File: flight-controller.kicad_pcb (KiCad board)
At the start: 2 copper layers, 51 x 54 mm, 32 parts, among them J1 XT60PW-M, J2 SM04B-SRSS-TB, J3 XT60PW-F, J4 XT60PW-F, J5 XT60PW-F, J6 XT60PW-F, U1 ACS773LCB-100B-PFF, U2 LMR33630ADDA, U3 AMS1117-3.3

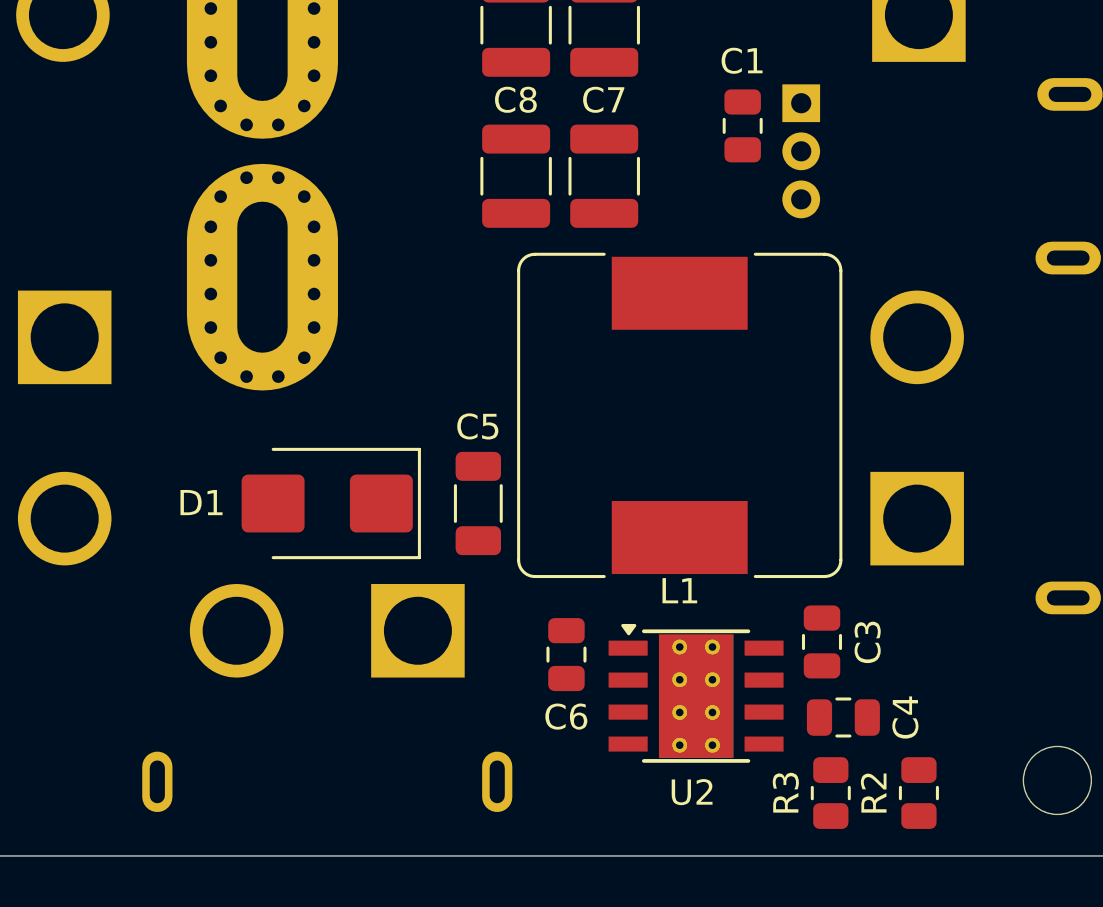
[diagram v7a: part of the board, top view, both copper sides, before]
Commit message: feat: Added VBAT plane
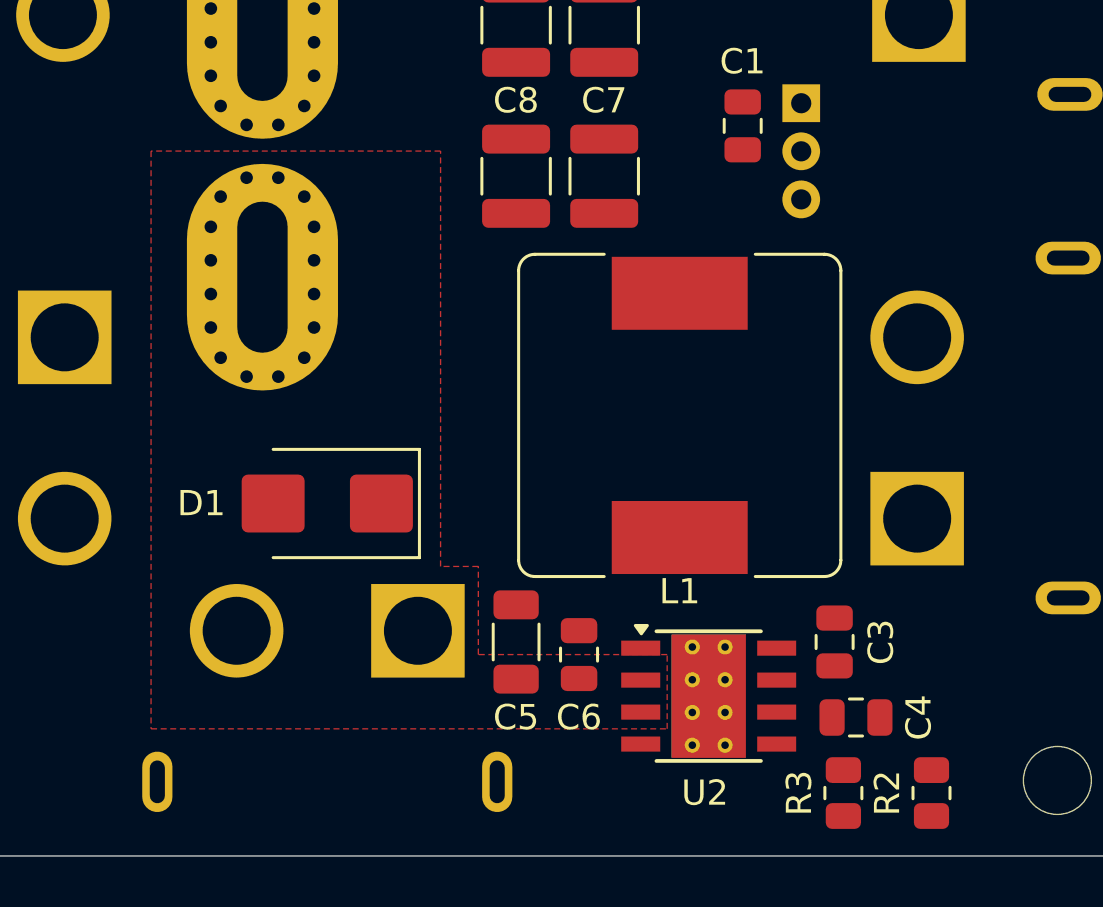
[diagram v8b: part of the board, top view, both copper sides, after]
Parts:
- moved C5 5.70 mm to (140.5, 124.5)
- moved C3 0.50 mm to (153.2, 124.5)
- moved C4 0.50 mm to (154.0, 127.5)
- moved C6 0.50 mm to (143.0, 125.0)
- moved R2 0.50 mm to (157.0, 130.5)
- moved R3 0.50 mm to (153.5, 130.5)
- moved U2 0.50 mm to (148.2, 126.7)
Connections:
- J1 pad SH1: unconnected-(J1-SHIELD-PadSH1) -> GND
- J1 pad SH2: unconnected-(J1-SHIELD-PadSH1) -> GND
- J3 pad SH1: unconnected-(J3-SHIELD-PadSH1) -> GND
- J3 pad SH2: unconnected-(J3-SHIELD-PadSH1) -> GND
- J4 pad SH1: unconnected-(J4-SHIELD-PadSH1) -> GND
- J4 pad SH2: unconnected-(J4-SHIELD-PadSH1) -> GND
- J5 pad SH1: unconnected-(J5-SHIELD-PadSH1) -> GND
- J5 pad SH2: unconnected-(J5-SHIELD-PadSH1) -> GND
- J6 pad SH1: unconnected-(J6-SHIELD-PadSH1) -> GND
- J6 pad SH2: unconnected-(J6-SHIELD-PadSH1) -> GND
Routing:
- added copper zone on F.Cu, net /VBAT
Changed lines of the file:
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@@
   (net 12 "Net-(U2-FB)")
   (net 13 "unconnected-(U2-PG-Pad4)")
-  (net 14 "unconnected-(J1-SHIELD-PadSH1)")
-  (net 15 "unconnected-(J3-SHIELD-PadSH1)")
-  (net 16 "unconnected-(J4-SHIELD-PadSH1)")
-  (net 17 "unconnected-(J5-SHIELD-PadSH1)")
-  (net 18 "unconnected-(J6-SHIELD-PadSH1)")
   (footprint "MountingHole:MountingHole_2.7mm_M2.5" (layer "F.Cu")
     (at 162 82)
@@
   )
   (footprint "Resistor_SMD:R_0805_2012Metric" (layer "F.Cu")
-    (at 153 130.5 -90)
+    (at 153.5 130.5 -90)
     (descr "Resistor SMD 0805 (2012 Metric), square (rectangular) end terminal, IPC_7351 nominal, (Body size source: IPC-SM-782 page 72, https://www.pcb-3d.com/wordpress/wp-content/uploads/ipc-sm-782a_amendment_1_and_2.pdf), generated with kicad-footprint-generator")
     (tags "resistor")
@@
   )
   (footprint "Capacitor_SMD:C_1206_3216Metric" (layer "F.Cu")
-    (at 139 119 90)
+    (at 140.5 124.5 90)
     (descr "Capacitor SMD 1206 (3216 Metric), square (rectangular) end terminal, IPC_7351 nominal, (Body size source: IPC-SM-782 page 76, https://www.pcb-3d.com/wordpress/wp-content/uploads/ipc-sm-782a_amendment_1_and_2.pdf), generated with kicad-footprint-generator")
     (tags "capacitor")
@@
     (property "ki_keywords" "cap capacitor")
     (attr smd)
-    (fp_text reference "C5" (at 3.025 0) (layer "F.SilkS")
+    (fp_text reference "C5" (at -3 0) (layer "F.SilkS")
         (effects (font (size 1 1) (thickness 0.15)))
     )
@@
   )
   (footprint "Resistor_SMD:R_0805_2012Metric" (layer "F.Cu")
-    (at 156.5 130.5 -90)
+    (at 157 130.5 -90)
     (descr "Resistor SMD 0805 (2012 Metric), square (rectangular) end terminal, IPC_7351 nominal, (Body size source: IPC-SM-782 page 72, https://www.pcb-3d.com/wordpress/wp-content/uploads/ipc-sm-782a_amendment_1_and_2.pdf), generated with kicad-footprint-generator")
     (tags "resistor")
@@
   )
   (footprint "Package_SO:Texas_HSOP-8-1EP_3.9x4.9mm_P1.27mm_ThermalVias" (layer "F.Cu")
-    (at 147.65 126.65)
+    (at 148.15 126.65)
     (descr "Texas Instruments HSOP 9, 1.27mm pitch, 3.9x4.9mm body, exposed pad, thermal vias, DDA0008J (http://www.ti.com/lit/ds/symlink/tps5430.pdf)")
     (tags "HSOP 1.27")
@@
   )
   (footprint "Capacitor_SMD:C_0805_2012Metric" (layer "F.Cu")
-    (at 142.5 125 90)
+    (at 143 125 90)
     (descr "Capacitor SMD 0805 (2012 Metric), square (rectangular) end terminal, IPC_7351 nominal, (Body size source: IPC-SM-782 page 76, https://www.pcb-3d.com/wordpress/wp-content/uploads/ipc-sm-782a_amendment_1_and_2.pdf, https://docs.google.com/spreadsheets/d/1BsfQQcO9C6DZCsRaXUlFlo91Tg2WpOkGARC1WS5S8t0/edit?usp=sharing), generated with kicad-footprint-generator")
     (tags "capacitor")
@@
   )
   (footprint "Capacitor_SMD:C_0805_2012Metric" (layer "F.Cu")
-    (at 153.5 127.5)
+    (at 154 127.5)
     (descr "Capacitor SMD 0805 (2012 Metric), square (rectangular) end terminal, IPC_7351 nominal, (Body size source: IPC-SM-782 page 76, https://www.pcb-3d.com/wordpress/wp-content/uploads/ipc-sm-782a_amendment_1_and_2.pdf, https://docs.google.com/spreadsheets/d/1BsfQQcO9C6DZCsRaXUlFlo91Tg2WpOkGARC1WS5S8t0/edit?usp=sharing), generated with kicad-footprint-generator")
     (tags "capacitor")
@@
   )
   (footprint "Capacitor_SMD:C_0805_2012Metric" (layer "F.Cu")
-    (at 152.65 124.5 90)
+    (at 153.15 124.5 90)
     (descr "Capacitor SMD 0805 (2012 Metric), square (rectangular) end terminal, IPC_7351 nominal, (Body size source: IPC-SM-782 page 76, https://www.pcb-3d.com/wordpress/wp-content/uploads/ipc-sm-782a_amendment_1_and_2.pdf, https://docs.google.com/spreadsheets/d/1BsfQQcO9C6DZCsRaXUlFlo91Tg2WpOkGARC1WS5S8t0/edit?usp=sharing), generated with kicad-footprint-generator")
     (tags "capacitor")
@@
       (net 2 "GND") (pinfunction "N") (pintype "passive") (solder_mask_margin 0.102))
     (pad "SH1" thru_hole oval (at -6.75 0 180) (size 1.2 2.4) (drill oval 0.6 1.7) (layers "*.Cu" "*.Mask")
-      (net 14 "unconnected-(J1-SHIELD-PadSH1)") (pinfunction "SHIELD") (pintype "passive+no_connect") (solder_mask_margin 0.102))
+      (net 2 "GND") (pinfunction "SHIELD") (pintype "passive+no_connect") (solder_mask_margin 0.102))
     (pad "SH2" thru_hole oval (at 6.75 0 180) (size 1.2 2.4) (drill oval 0.6 1.7) (layers "*.Cu" "*.Mask")
-      (net 14 "unconnected-(J1-SHIELD-PadSH1)") (pinfunction "SHIELD") (pintype "passive+no_connect") (solder_mask_margin 0.102))
+      (net 2 "GND") (pinfunction "SHIELD") (pintype "passive+no_connect") (solder_mask_margin 0.102))
     (model "${KIPRJMOD}/lib/3d_models/XT60PW-M.step"
       (offset (xyz 0 0 0))
@@
       (net 2 "GND") (pinfunction "N") (pintype "passive") (solder_mask_margin 0.102))
     (pad "SH1" thru_hole oval (at -6.75 -6 90) (size 1.3 2.6) (drill oval 0.6 1.7) (layers "*.Cu" "*.Mask")
-      (net 16 "unconnected-(J4-SHIELD-PadSH1)") (pinfunction "SHIELD") (pintype "passive+no_connect") (solder_mask_margin 0.102))
+      (net 2 "GND") (pinfunction "SHIELD") (pintype "passive+no_connect") (solder_mask_margin 0.102))
     (pad "SH2" thru_hole oval (at 6.75 -6 90) (size 1.3 2.6) (drill oval 0.6 1.7) (layers "*.Cu" "*.Mask")
-      (net 16 "unconnected-(J4-SHIELD-PadSH1)") (pinfunction "SHIELD") (pintype "passive+no_connect") (solder_mask_margin 0.102))
+      (net 2 "GND") (pinfunction "SHIELD") (pintype "passive+no_connect") (solder_mask_margin 0.102))
     (model "${KIPRJMOD}/lib/3d_models/XT60PW-F.step"
       (offset (xyz 0 0 0))
@@
       (net 2 "GND") (pinfunction "N") (pintype "passive") (solder_mask_margin 0.102))
     (pad "SH1" thru_hole oval (at -6.75 -6 270) (size 1.3 2.6) (drill oval 0.6 1.7) (layers "*.Cu" "*.Mask")
-      (net 18 "unconnected-(J6-SHIELD-PadSH1)") (pinfunction "SHIELD") (pintype "passive+no_connect") (solder_mask_margin 0.102))
+      (net 2 "GND") (pinfunction "SHIELD") (pintype "passive+no_connect") (solder_mask_margin 0.102))
     (pad "SH2" thru_hole oval (at 6.75 -6 270) (size 1.3 2.6) (drill oval 0.6 1.7) (layers "*.Cu" "*.Mask")
-      (net 18 "unconnected-(J6-SHIELD-PadSH1)") (pinfunction "SHIELD") (pintype "passive+no_connect") (solder_mask_margin 0.102))
+      (net 2 "GND") (pinfunction "SHIELD") (pintype "passive+no_connect") (solder_mask_margin 0.102))
     (model "${KIPRJMOD}/lib/3d_models/XT60PW-F.step"
       (offset (xyz 0 0 0))
@@
       (net 2 "GND") (pinfunction "N") (pintype "passive") (solder_mask_margin 0.102))
     (pad "SH1" thru_hole oval (at -6.75 -6 90) (size 1.3 2.6) (drill oval 0.6 1.7) (layers "*.Cu" "*.Mask")
-      (net 15 "unconnected-(J3-SHIELD-PadSH1)") (pinfunction "SHIELD") (pintype "passive+no_connect") (solder_mask_margin 0.102))
+      (net 2 "GND") (pinfunction "SHIELD") (pintype "passive+no_connect") (solder_mask_margin 0.102))
     (pad "SH2" thru_hole oval (at 6.75 -6 90) (size 1.3 2.6) (drill oval 0.6 1.7) (layers "*.Cu" "*.Mask")
-      (net 15 "unconnected-(J3-SHIELD-PadSH1)") (pinfunction "SHIELD") (pintype "passive+no_connect") (solder_mask_margin 0.102))
+      (net 2 "GND") (pinfunction "SHIELD") (pintype "passive+no_connect") (solder_mask_margin 0.102))
     (model "${KIPRJMOD}/lib/3d_models/XT60PW-F.step"
       (offset (xyz 0 0 0))
@@
       (net 2 "GND") (pinfunction "N") (pintype "passive") (solder_mask_margin 0.102))
     (pad "SH1" thru_hole oval (at -6.75 -6 270) (size 1.3 2.6) (drill oval 0.6 1.7) (layers "*.Cu" "*.Mask")
-      (net 17 "unconnected-(J5-SHIELD-PadSH1)") (pinfunction "SHIELD") (pintype "passive+no_connect") (solder_mask_margin 0.102))
+      (net 2 "GND") (pinfunction "SHIELD") (pintype "passive+no_connect") (solder_mask_margin 0.102))
     (pad "SH2" thru_hole oval (at 6.75 -6 270) (size 1.3 2.6) (drill oval 0.6 1.7) (layers "*.Cu" "*.Mask")
-      (net 17 "unconnected-(J5-SHIELD-PadSH1)") (pinfunction "SHIELD") (pintype "passive+no_connect") (solder_mask_margin 0.102))
+      (net 2 "GND") (pinfunction "SHIELD") (pintype "passive+no_connect") (solder_mask_margin 0.102))
     (model "${KIPRJMOD}/lib/3d_models/XT60PW-F.step"
       (offset (xyz 0 0 0))
@@
   (gr_rect (start 114 79) (end 165 133)
     (stroke (width 0.05) (type default)) (fill none) (layer "Edge.Cuts"))
+  (zone (net 7) (net_name "/VBAT") (layer "F.Cu") (hatch edge 0.5)
+    (connect_pads yes (clearance 0.5))
+    (min_thickness 0.5) (filled_areas_thickness no)
+    (fill yes (thermal_gap 0.5) (thermal_bridge_width 0.5))
+    (polygon
+      (pts
+        (xy 126 105)
+        (xy 126 127.95)
+        (xy 146.5 127.95)
+        (xy 146.5 125)
+        (xy 139 125)
+        (xy 139 121.5)
+        (xy 137.5 121.5)
+        (xy 137.5 113.5)
+        (xy 137.5 113.5)
+        (xy 137.5 105)
+      )
+    )
+  )
 )
